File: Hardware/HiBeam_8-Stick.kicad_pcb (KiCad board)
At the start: 2 copper layers, 59.1 x 14.6 mm, 20 parts, among them J1 CONN_041X04_NO_SILK, J2 CONN_041X04_NO_SILK, U1 APA102, U2 APA102, U3 APA102, U4 APA102, U5 APA102, U6 APA102, U7 APA102, U8 APA102

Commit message: Fixed silk.
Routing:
- net +5V: track 100.6 -> 101.7 mm
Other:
- board text added: "HiBeams 8-Stick"
- board text removed: "HiBeam 8-Stick"
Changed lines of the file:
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@@
     (thickness 1.6)
     (drawings 45)
-    (tracks 183)
+    (tracks 187)
     (zones 0)
     (modules 20)
@@
   )
   (setup
-    (last_trace_width 0.25)
+    (last_trace_width 0.4064)
     (user_trace_width 0.2032)
     (user_trace_width 0.254)
@@
     (effects (font (size 1.5 1.5) (thickness 0.3)))
   )
-  (gr_text "HiBeam 8-Stick" (at 186.69 189.484) (layer Cmts.User)
+  (gr_text "HiBeams 8-Stick" (at 186.69 189.484) (layer Cmts.User)
     (effects (font (size 1.5 1.5) (thickness 0.3)) (justify left))
   )
@@
     (arrow2b (pts (xy 178.3334 116.205) (xy 177.206896 116.791421)))
   )
-  (gr_text "HiBeam 8-Stick" (at 148.8186 103.886) (layer B.SilkS)
-    (effects (font (size 1.27 1.27) (thickness 0.2032)) (justify mirror))
+  (gr_text "HiBeams 8-Stick" (at 148.8186 103.886) (layer B.SilkS)
+    (effects (font (size 1.5 1.5) (thickness 0.299999)) (justify mirror))
   )
   (gr_line (start 119.2784 107.95) (end 178.3334 107.95) (angle 90) (layer Edge.Cuts) (width 0.15))
@@
   (segment (start 129.6416 102.0064) (end 129.643399 102.0064) (width 0.4064) (layer F.Cu) (net 1))
   (segment (start 129.643399 100.47) (end 129.643399 102.0064) (width 0.4064) (layer F.Cu) (net 1))
+  (via (at 155.7782 105.283) (size 0.8) (drill 0.4) (layers F.Cu B.Cu) (net 2))
+  (segment (start 155.7782 103.71836) (end 155.7782 105.283) (width 0.4064) (layer F.Cu) (net 2))
+  (segment (start 155.7782 105.283) (end 155.7782 105.41) (width 0.4064) (layer B.Cu) (net 2))
+  (segment (start 141.8336 103.71836) (end 141.8336 105.1306) (width 0.4064) (layer F.Cu) (net 2))
+  (segment (start 141.8336 105.1306) (end 141.8336 105.41) (width 0.4064) (layer B.Cu) (net 2))
+  (via (at 141.8336 105.1306) (size 0.8) (drill 0.4) (layers F.Cu B.Cu) (net 2))
   (segment (start 167.9684 100.47) (end 167.9684 102.6904) (width 0.4064) (layer F.Cu) (net 2))
   (segment (start 167.9684 102.6904) (end 168.99636 103.71836) (width 0.4064) (layer F.Cu) (net 2))
@@
   (segment (start 124.46 105.41) (end 127.8636 105.41) (width 3.81) (layer B.Cu) (net 2))
   (segment (start 127.8636 105.41) (end 141.8336 105.41) (width 3.81) (layer B.Cu) (net 2))
+  (segment (start 141.8336 105.41) (end 141.8336 105.41) (width 3.81) (layer B.Cu) (net 2))
   (segment (start 141.8336 105.41) (end 155.7782 105.41) (width 3.81) (layer B.Cu) (net 2))
+  (segment (start 155.7782 105.41) (end 155.7782 105.41) (width 3.81) (layer B.Cu) (net 2))
   (segment (start 155.7782 105.41) (end 169.7482 105.41) (width 3.81) (layer B.Cu) (net 2))
   (segment (start 169.7482 105.41) (end 172.72 105.41) (width 3.81) (layer B.Cu) (net 2))
@@
   (via (at 169.7482 104.8766) (size 0.8) (drill 0.4) (layers F.Cu B.Cu) (net 2))
   (segment (start 169.7482 104.8766) (end 169.7482 105.41) (width 0.4064) (layer B.Cu) (net 2))
-  (segment (start 155.7782 103.71836) (end 155.7782 104.8766) (width 0.4064) (layer F.Cu) (net 2))
-  (via (at 155.7782 104.8766) (size 0.8) (drill 0.4) (layers F.Cu B.Cu) (net 2))
   (segment (start 155.7782 104.8766) (end 155.7782 105.41) (width 0.4064) (layer B.Cu) (net 2))
-  (segment (start 141.8336 103.71836) (end 141.8336 104.8512) (width 0.4064) (layer F.Cu) (net 2))
-  (via (at 141.8336 104.8512) (size 0.8) (drill 0.4) (layers F.Cu B.Cu) (net 2))
   (segment (start 141.8336 104.8512) (end 141.8336 105.41) (width 0.4064) (layer B.Cu) (net 2))
   (segment (start 127.8636 103.71836) (end 127.8636 104.8766) (width 0.4064) (layer F.Cu) (net 2))

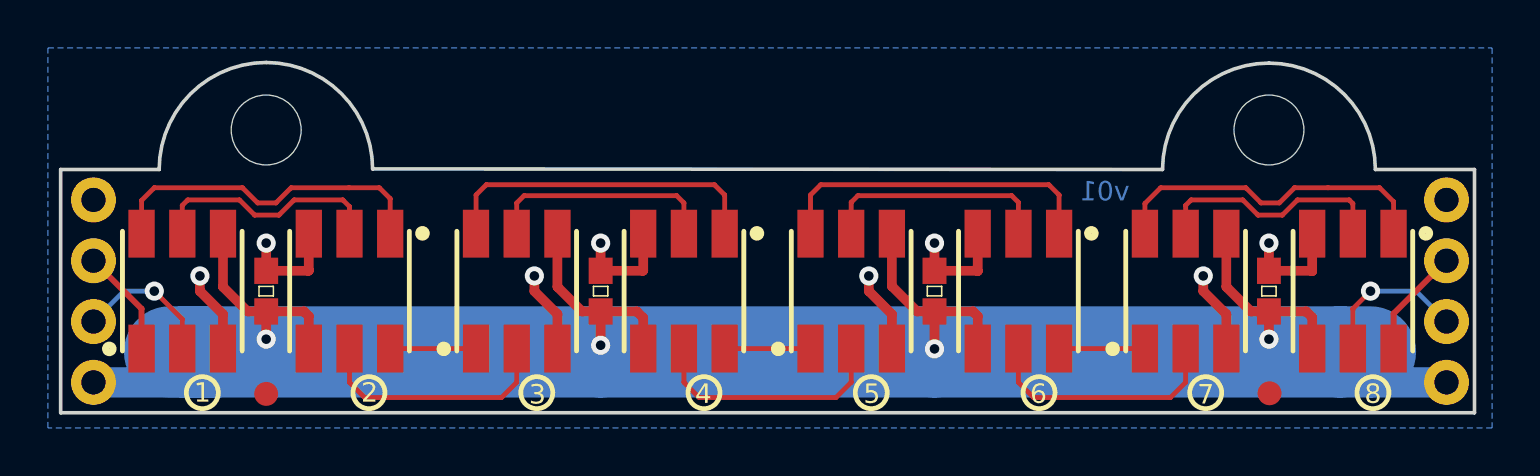
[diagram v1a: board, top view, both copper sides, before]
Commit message: Castleated connectors.
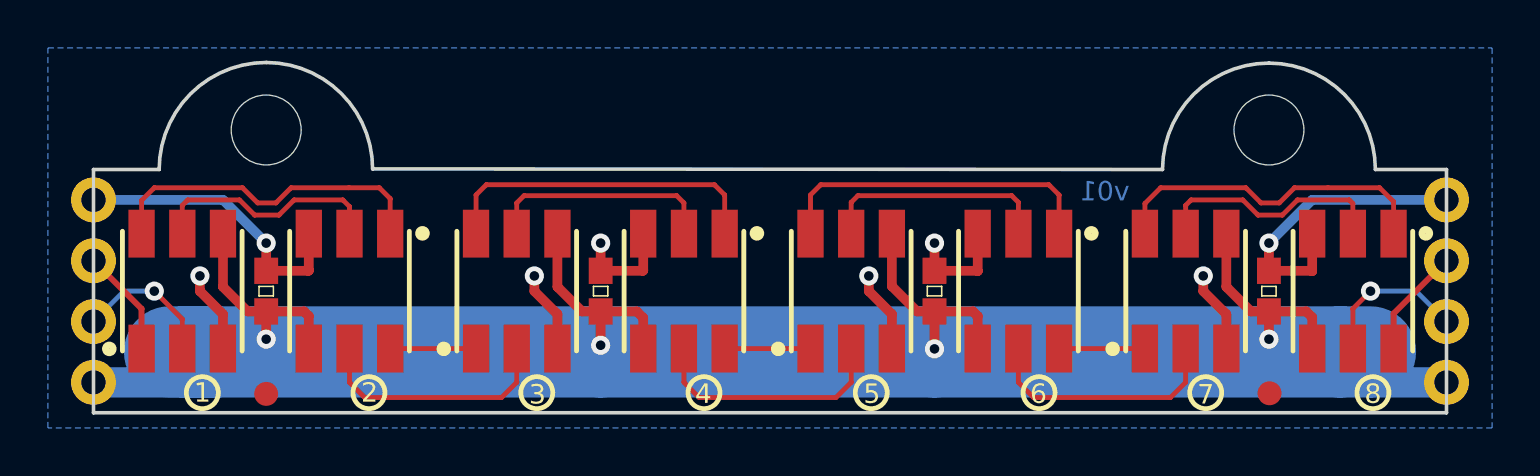
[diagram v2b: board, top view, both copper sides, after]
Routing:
- net GND: track 31.8 -> 47.9 mm
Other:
- board size 59.1 x 14.6 mm -> 56.5 x 14.6 mm
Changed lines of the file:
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@@
     (links 44)
     (no_connects 0)
-    (area 108.026286 87.292311 239.952514 194.4858)
+    (area 107.264286 87.292311 239.952514 194.4858)
     (thickness 1.6)
     (drawings 45)
-    (tracks 187)
+    (tracks 191)
     (zones 0)
     (modules 20)
@@
     (pad "" np_thru_hole circle (at 0 0) (size 2.921 2.921) (drill 2.921) (layers *.Cu *.Mask))
   )
+  (dimension 14.605 (width 0.3) (layer Dwgs.User)
+    (gr_text "0.5750 in" (at 112.95 100.6475 270) (layer Dwgs.User)
+      (effects (font (size 1.5 1.5) (thickness 0.3)))
+    )
+    (feature1 (pts (xy 120.65 107.95) (xy 111.6 107.95)))
+    (feature2 (pts (xy 120.65 93.345) (xy 111.6 93.345)))
+    (crossbar (pts (xy 114.3 93.345) (xy 114.3 107.95)))
+    (arrow1a (pts (xy 114.3 107.95) (xy 113.713579 106.823496)))
+    (arrow1b (pts (xy 114.3 107.95) (xy 114.886421 106.823496)))
+    (arrow2a (pts (xy 114.3 93.345) (xy 113.713579 94.471504)))
+    (arrow2b (pts (xy 114.3 93.345) (xy 114.886421 94.471504)))
+  )
+  (dimension 56.515 (width 0.3) (layer Dwgs.User)
+    (gr_text "2.2250 in" (at 148.9075 113.999) (layer Dwgs.User)
+      (effects (font (size 1.5 1.5) (thickness 0.3)))
+    )
+    (feature1 (pts (xy 120.65 107.95) (xy 120.65 115.349)))
+    (feature2 (pts (xy 177.165 107.95) (xy 177.165 115.349)))
+    (crossbar (pts (xy 177.165 112.649) (xy 120.65 112.649)))
+    (arrow1a (pts (xy 120.65 112.649) (xy 121.776504 112.062579)))
+    (arrow1b (pts (xy 120.65 112.649) (xy 121.776504 113.235421)))
+    (arrow2a (pts (xy 177.165 112.649) (xy 176.038496 112.062579)))
+    (arrow2b (pts (xy 177.165 112.649) (xy 176.038496 113.235421)))
+  )
+  (gr_line (start 177.165 97.79) (end 177.165 107.95) (angle 90) (layer Edge.Cuts) (width 0.15))
+  (gr_line (start 120.65 97.79) (end 120.65 107.95) (angle 90) (layer Edge.Cuts) (width 0.15))
+  (gr_line (start 120.65 97.79) (end 123.3932 97.79) (angle 90) (layer Edge.Cuts) (width 0.15))
+  (gr_line (start 120.65 107.95) (end 177.165 107.95) (angle 90) (layer Edge.Cuts) (width 0.15))
   (dimension 10.16 (width 0.3) (layer Dwgs.User)
     (gr_text "0.4000 in" (at 185.5254 102.87 90) (layer Dwgs.User)
@@
     (arrow2b (pts (xy 184.1754 107.95) (xy 183.588979 106.823496)))
   )
-  (dimension 14.6304 (width 0.3) (layer Dwgs.User)
-    (gr_text "0.5760 in" (at 113.712 100.6348 90) (layer Dwgs.User)
-      (effects (font (size 1.5 1.5) (thickness 0.3)))
-    )
-    (feature1 (pts (xy 119.2784 93.3196) (xy 112.362 93.3196)))
-    (feature2 (pts (xy 119.2784 107.95) (xy 112.362 107.95)))
-    (crossbar (pts (xy 115.062 107.95) (xy 115.062 93.3196)))
-    (arrow1a (pts (xy 115.062 93.3196) (xy 115.648421 94.446104)))
-    (arrow1b (pts (xy 115.062 93.3196) (xy 114.475579 94.446104)))
-    (arrow2a (pts (xy 115.062 107.95) (xy 115.648421 106.823496)))
-    (arrow2b (pts (xy 115.062 107.95) (xy 114.475579 106.823496)))
-  )
   (dimension 41.884608 (width 0.3) (layer Dwgs.User)
     (gr_text "1.6490 in" (at 148.808736 88.65501 359.9652542) (layer Dwgs.User)
@@
     (arrow2b (pts (xy 127.865618 89.99231) (xy 128.992477 89.406573)))
   )
-  (gr_line (start 174.1932 97.79) (end 178.3334 97.79) (angle 90) (layer Edge.Cuts) (width 0.15))
+  (gr_line (start 174.1932 97.79) (end 177.165 97.79) (angle 90) (layer Edge.Cuts) (width 0.15))
   (gr_line (start 132.3086 97.7646) (end 165.3032 97.79) (angle 90) (layer Edge.Cuts) (width 0.15))
-  (gr_line (start 119.2784 97.79) (end 123.3932 97.79) (angle 90) (layer Edge.Cuts) (width 0.15))
   (gr_arc (start 169.7482 97.79) (end 165.3032 97.79) (angle 90) (layer Edge.Cuts) (width 0.15))
   (gr_arc (start 169.7482 97.79) (end 169.7482 93.345) (angle 90) (layer Edge.Cuts) (width 0.15))
@@
     (effects (font (size 0.8128 0.8128) (thickness 0.2032)) (justify mirror))
   )
-  (dimension 59.055 (width 0.3) (layer Dwgs.User)
-    (gr_text "2.3250 in" (at 148.8059 117.555) (layer Dwgs.User)
-      (effects (font (size 1.5 1.5) (thickness 0.3)))
-    )
-    (feature1 (pts (xy 119.2784 107.95) (xy 119.2784 118.905)))
-    (feature2 (pts (xy 178.3334 107.95) (xy 178.3334 118.905)))
-    (crossbar (pts (xy 178.3334 116.205) (xy 119.2784 116.205)))
-    (arrow1a (pts (xy 119.2784 116.205) (xy 120.404904 115.618579)))
-    (arrow1b (pts (xy 119.2784 116.205) (xy 120.404904 116.791421)))
-    (arrow2a (pts (xy 178.3334 116.205) (xy 177.206896 115.618579)))
-    (arrow2b (pts (xy 178.3334 116.205) (xy 177.206896 116.791421)))
-  )
   (gr_text "HiBeams 8-Stick" (at 148.8186 103.886) (layer B.SilkS)
     (effects (font (size 1.5 1.5) (thickness 0.299999)) (justify mirror))
   )
-  (gr_line (start 119.2784 107.95) (end 178.3334 107.95) (angle 90) (layer Edge.Cuts) (width 0.15))
-  (gr_line (start 178.3334 107.95) (end 178.3334 97.79) (angle 90) (layer Edge.Cuts) (width 0.15))
-  (gr_line (start 119.2784 97.79) (end 119.2784 107.95) (angle 90) (layer Edge.Cuts) (width 0.15))
+  (segment (start 120.65 99.06) (end 126.0602 99.06) (width 0.4064) (layer B.Cu) (net 1))
+  (via (at 127.8636 100.8634) (size 0.8) (drill 0.4) (layers F.Cu B.Cu) (net 1))
+  (segment (start 127.8636 100.8634) (end 127.8636 102.02164) (width 0.4064) (layer F.Cu) (net 1))
+  (segment (start 126.0602 99.06) (end 127.8636 100.8634) (width 0.4064) (layer B.Cu) (net 1))
+  (segment (start 177.165 99.06) (end 171.5516 99.06) (width 0.4064) (layer B.Cu) (net 1))
+  (via (at 169.7482 100.8634) (size 0.8) (drill 0.4) (layers F.Cu B.Cu) (net 1))
+  (segment (start 169.7482 100.8634) (end 169.7482 102.02164) (width 0.4064) (layer F.Cu) (net 1))
+  (segment (start 171.5516 99.06) (end 169.7482 100.8634) (width 0.4064) (layer B.Cu) (net 1))
   (segment (start 126.058401 105.27) (end 126.058401 103.833401) (width 0.4064) (layer F.Cu) (net 1))
   (segment (start 126.058401 103.833401) (end 125.095 102.87) (width 0.4064) (layer F.Cu) (net 1))
@@
   (segment (start 139.065 102.87) (end 139.065 102.235) (width 0.4064) (layer F.Cu) (net 1))
   (via (at 139.065 102.235) (size 0.8) (drill 0.4) (layers F.Cu B.Cu) (net 1))
-  (segment (start 169.7482 102.02164) (end 169.7482 100.8634) (width 0.4064) (layer F.Cu) (net 1))
-  (via (at 169.7482 100.8634) (size 0.8) (drill 0.4) (layers F.Cu B.Cu) (net 1))
   (segment (start 155.7782 102.02164) (end 155.7782 100.8634) (width 0.4064) (layer F.Cu) (net 1))
   (via (at 155.7782 100.8634) (size 0.8) (drill 0.4) (layers F.Cu B.Cu) (net 1))
   (segment (start 141.8336 102.02164) (end 141.8336 100.8634) (width 0.4064) (layer F.Cu) (net 1))
   (via (at 141.8336 100.8634) (size 0.8) (drill 0.4) (layers F.Cu B.Cu) (net 1))
-  (segment (start 127.8636 102.02164) (end 127.8636 100.8634) (width 0.4064) (layer F.Cu) (net 1))
-  (via (at 127.8636 100.8634) (size 0.8) (drill 0.4) (layers F.Cu B.Cu) (net 1))
   (segment (start 169.7482 102.02164) (end 171.54144 102.02164) (width 0.4064) (layer F.Cu) (net 1))
   (segment (start 171.54144 102.02164) (end 171.5516 102.0318) (width 0.4064) (layer F.Cu) (net 1))
